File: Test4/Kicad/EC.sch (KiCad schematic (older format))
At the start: 26 parts, among them U1 MCP6244, U2 MCP6241

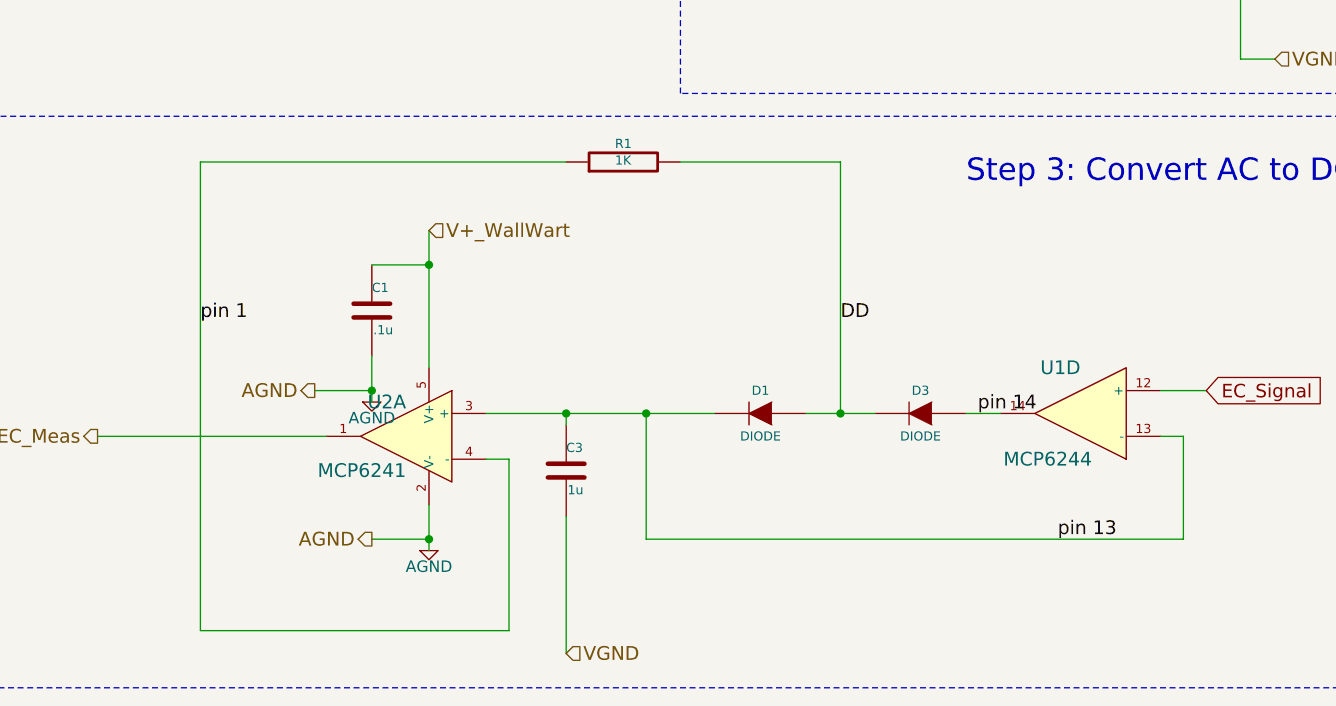
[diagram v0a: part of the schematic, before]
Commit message: fixed mistake in schematic/layout for AD to DC conversion
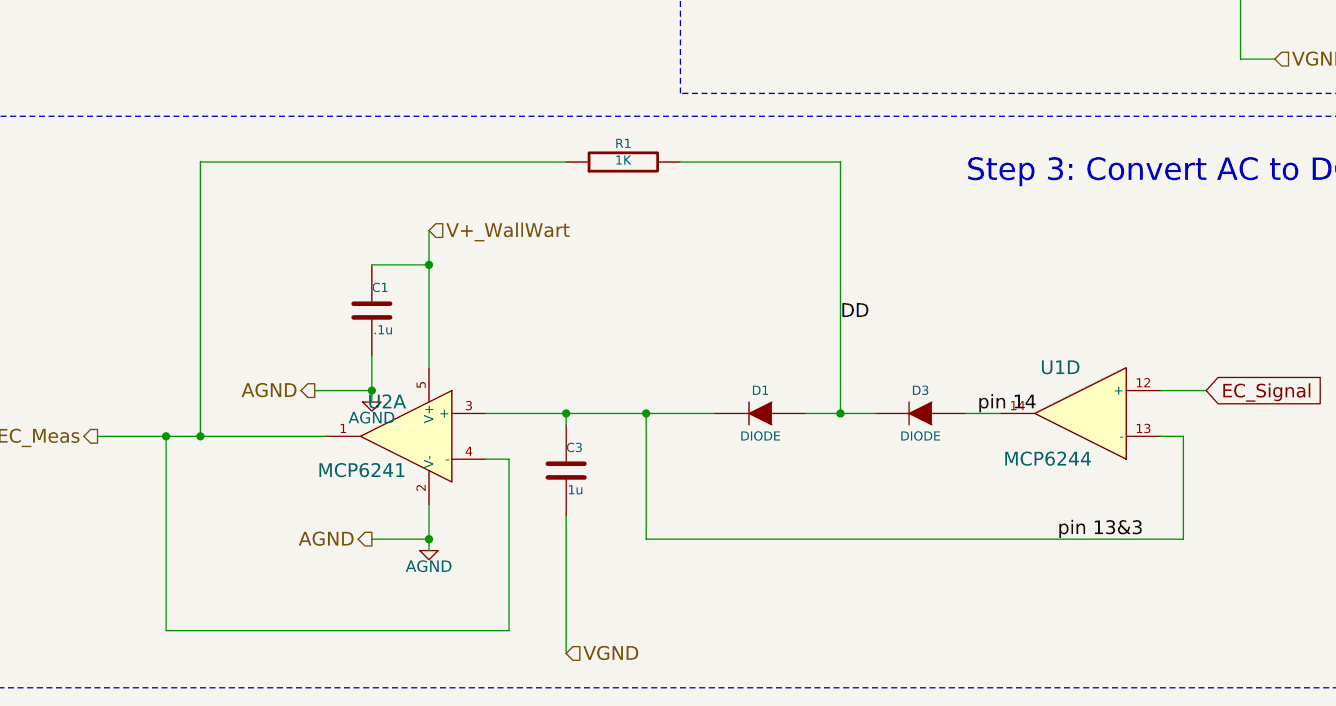
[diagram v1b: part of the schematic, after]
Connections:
- net pin 1 is gone; now on net EC_Meas: R1.1, U2.4 (-)
- net pin 13 renamed pin 13&3
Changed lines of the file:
@@
 Sheet 2 2
 Title ""
-Date "8 dec 2014"
+Date "10 dec 2014"
 Rev ""
 Comp ""
@@
 	3150 6100 3150 6850
 Wire Wire Line
-	3150 6850 1800 6850
-Wire Wire Line
-	1800 6850 1800 4800
+	3150 6850 1650 6850
 $Comp
 L R R1
@@
 EC_Meas
 Text Label 5550 6450 0    60   ~ 0
-pin 13
+pin 13&3
 Text Label 5200 5900 0    60   ~ 0
 pin 14
 Text Label 4600 5500 0    60   ~ 0
 DD
-Text Label 1800 5500 0    60   ~ 0
-pin 1
+Wire Wire Line
+	1800 4800 1800 6000
+Connection ~ 1800 6000
+Wire Wire Line
+	1650 6850 1650 6000
+Connection ~ 1650 6000
 $EndSCHEMATC
